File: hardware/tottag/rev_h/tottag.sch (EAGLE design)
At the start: 208 parts, among them J1 USB4110-GF-A, J2 DM3AT-SF-PEJM5, J3 TC2030-JLINK-NL-2SIDE, J4 TC2030-JLINK-NL-2SIDE, J5 MOLEX-PICO-SPOX-3SIDE, Q1 CSD75207W15, Q2 CSD75207W15, T1 HHM1595A1, U1 DW1000, U10 STM32F091CC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

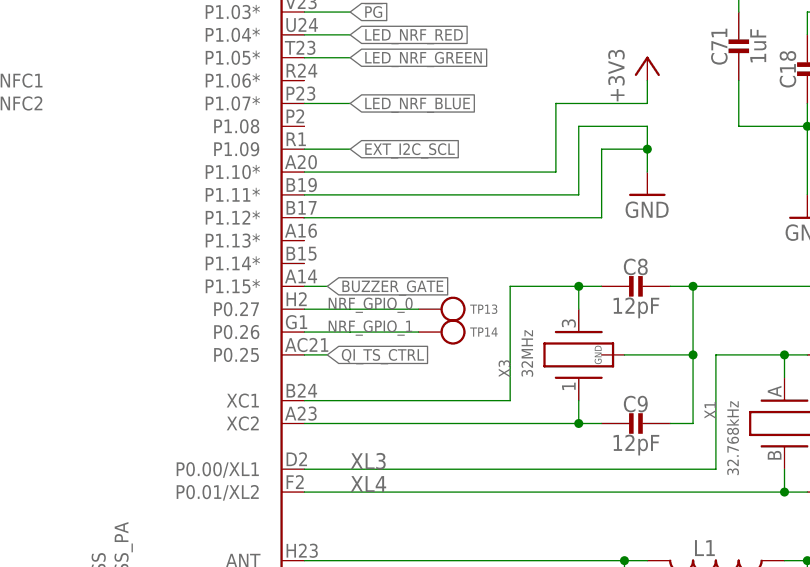
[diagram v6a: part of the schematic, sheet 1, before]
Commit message: rev_h: Connect STM PA0 to allow STANDBY wake
Slightly unclear whether STM should allow for STANDBY wake from any
of the WKUP pins, but some forum posts indicate that it can actually
only be done from WKUP1 for STANDBY mode. In either case, another
GPIO link between the two micro's isn't a huge deal.

This does sacrifice the GPIO1 test point from the nRF, because getting
at any other pin would've been insane.
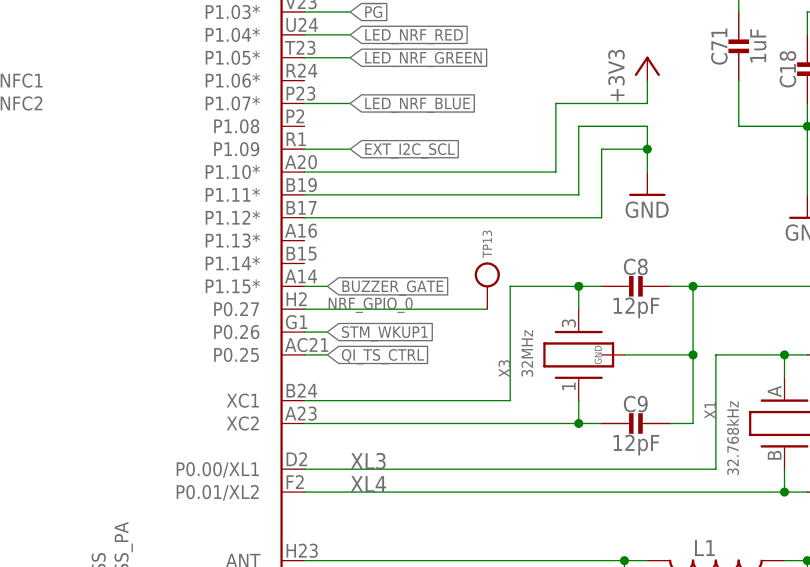
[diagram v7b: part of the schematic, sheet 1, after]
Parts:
- removed TP14: TEST-POINT, headers:TEST-POINT
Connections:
- removed net NRF_GPIO_1: TP14.TESTPOINT, U7.P0.26
- new net STM_WKUP1: U10.PA0, U7.P0.26
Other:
- note added: "Only PA0 can wake from STANDBY mode"
- moved on the sheet: TP13
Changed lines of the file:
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@@
 </part>
 <part name="TP13" library="headers" deviceset="TEST-POINT" device=""/>
-<part name="TP14" library="headers" deviceset="TEST-POINT" device=""/>
 <part name="FRAME3" library="lab11-frames" deviceset="LETTER_L_BLANK" device=""/>
 <part name="U10" library="chips" library_urn="urn:adsk.eagle:library:20878352" deviceset="STM32F091CC" device="" package3d_urn="urn:adsk.eagle:package:20878823/2"/>
@@
 <attribute name="VALUE" x="36.83" y="110.49" size="1.778" layer="96" ratio="12" rot="R270" align="bottom-center"/>
 </instance>
-<instance part="TP13" gate="G$1" x="121.92" y="68.58" smashed="yes" rot="R180">
-<attribute name="NAME" x="125.095" y="68.58" size="1.016" layer="95" ratio="12" rot="R180" align="center-right"/>
-</instance>
-<instance part="TP14" gate="G$1" x="121.92" y="66.04" smashed="yes" rot="R180">
-<attribute name="NAME" x="125.095" y="66.04" size="1.016" layer="95" ratio="12" rot="R180" align="center-right"/>
+<instance part="TP13" gate="G$1" x="127" y="71.12" smashed="yes" rot="R270">
+<attribute name="NAME" x="127" y="74.295" size="1.016" layer="95" ratio="12" rot="R270" align="center-right"/>
 </instance>
 <instance part="TP15" gate="G$1" x="96.52" y="144.78" smashed="yes" rot="R180">
@@
 </segment>
 </net>
-<net name="NRF_GPIO_1" class="0">
-<segment>
-<pinref part="U7" gate="G$1" pin="P0.26"/>
-<wire x1="106.68" y1="66.04" x2="111.76" y2="66.04" width="0.1524" layer="91"/>
-<pinref part="TP14" gate="G$1" pin="TESTPOINT"/>
-<wire x1="111.76" y1="66.04" x2="119.38" y2="66.04" width="0.1524" layer="91"/>
-<label x="109.22" y="66.04" size="1.27" layer="95"/>
-</segment>
-</net>
 <net name="NRF_GPIO_0" class="0">
 <segment>
 <pinref part="U7" gate="G$1" pin="P0.27"/>
-<wire x1="106.68" y1="68.58" x2="111.76" y2="68.58" width="0.1524" layer="91"/>
 <pinref part="TP13" gate="G$1" pin="TESTPOINT"/>
-<wire x1="111.76" y1="68.58" x2="119.38" y2="68.58" width="0.1524" layer="91"/>
+<wire x1="106.68" y1="68.58" x2="127" y2="68.58" width="0.1524" layer="91"/>
 <label x="109.22" y="68.58" size="1.27" layer="95"/>
 </segment>
@@
 </segment>
 </net>
+<net name="STM_WKUP1" class="0">
+<segment>
+<pinref part="U7" gate="G$1" pin="P0.26"/>
+<wire x1="109.22" y1="66.04" x2="106.68" y2="66.04" width="0.1524" layer="91"/>
+<label x="109.22" y="66.04" size="1.27" layer="95" xref="yes"/>
+</segment>
+</net>
 </nets>
 </sheet>
@@
 <text x="38.1" y="2.54" size="2.032" layer="98" rot="R180" align="center">2x Programming header (top/bot)</text>
 <text x="151.13" y="87.63" size="1.27" layer="98" rot="R90">1% tol</text>
+<text x="71.12" y="132.334" size="0.762" layer="98">Only PA0 can wake from STANDBY mode</text>
 </plain>
 <instances>
@@
 </segment>
 </net>
+<net name="STM_WKUP1" class="0">
+<segment>
+<pinref part="U10" gate="U1" pin="PA0"/>
+<wire x1="71.12" y1="106.68" x2="71.12" y2="132.08" width="0.1524" layer="91"/>
+<wire x1="71.12" y1="132.08" x2="111.76" y2="132.08" width="0.1524" layer="91"/>
+<label x="111.76" y="132.08" size="1.27" layer="95" xref="yes"/>
+</segment>
+</net>

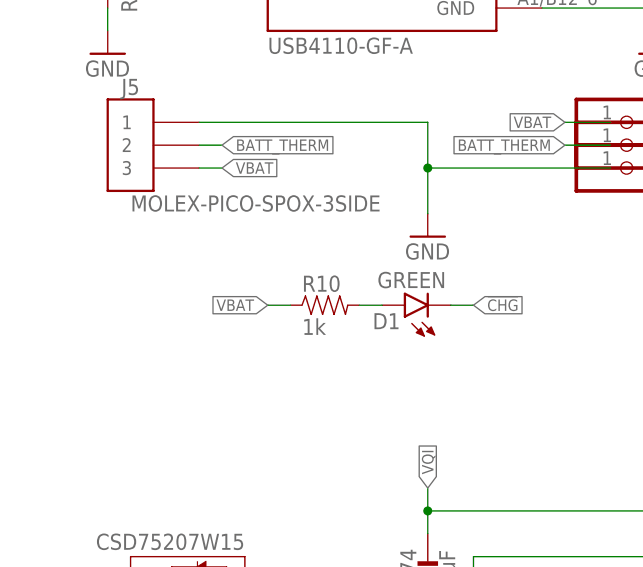
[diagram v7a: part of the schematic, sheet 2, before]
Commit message: rev_h: tie !CHG LED to +3v3
This means the LED won't power on to indicate charging if the device
is switched off, but that's an uncommon case anyway. We may even end
up just DNP'ing the CHG LED; it's of middling use; in which case an
internal nRF pull-up can be used in place of this for the !CHG net.
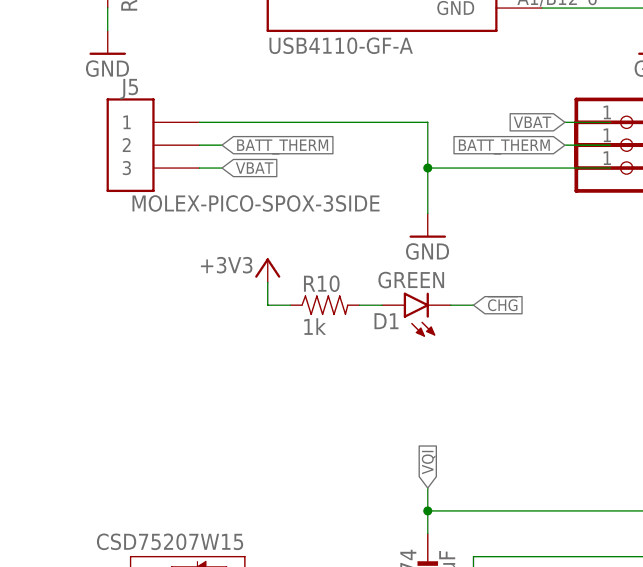
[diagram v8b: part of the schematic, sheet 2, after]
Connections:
- net +3V3: now also R10.1
- net VBAT: no longer R10.1
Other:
- note added: "Caution: The !CHG network connects to a GPIO pin on the nRF, which can leak power through the ESD pins when the nRF is not energized (i.e. don't drive this LED from VBAT!)"
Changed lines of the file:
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@@
 <part name="TP26" library="headers" deviceset="TEST-POINT" device=""/>
 <part name="TP27" library="headers" deviceset="TEST-POINT" device=""/>
+<part name="P+8" library="regulators" deviceset="+3V3" device=""/>
 </parts>
 <sheets>
@@
 the connector (metal contacts of the connector
 not visible), the wires from L to R are [-, NTC, +]</text>
+<text x="24.384" y="124.206" size="0.8128" layer="98" align="top-right">Caution: The !CHG network
+connects to a GPIO pin on the
+nRF, which can leak power
+through the ESD pins when the
+nRF is not energized (i.e. don't
+drive this LED from VBAT!)</text>
 </plain>
 <instances>
@@
 <attribute name="NAME" x="68.326" y="137.287" size="1.778" layer="95"/>
 <attribute name="VALUE" x="59.69" y="132.08" size="1.778" layer="96"/>
+</instance>
+<instance part="P+8" gate="P1" x="25.4" y="127" smashed="yes">
+<attribute name="VALUE" x="23.876" y="127.254" size="1.778" layer="96" rot="R180"/>
 </instance>
 </instances>
@@
 <wire x1="20.32" y1="33.02" x2="15.24" y2="33.02" width="0.1524" layer="91"/>
 </segment>
+<segment>
+<pinref part="R10" gate="G$1" pin="1"/>
+<wire x1="27.94" y1="121.92" x2="25.4" y2="121.92" width="0.1524" layer="91"/>
+<wire x1="25.4" y1="121.92" x2="25.4" y2="124.46" width="0.1524" layer="91"/>
+<pinref part="P+8" gate="P1" pin="+3V3"/>
+</segment>
 </net>
 <net name="VBAT" class="0">
@@
 </segment>
 <segment>
-<pinref part="R10" gate="G$1" pin="1"/>
-<wire x1="25.4" y1="121.92" x2="27.94" y2="121.92" width="0.1524" layer="91"/>
-<label x="25.4" y="121.92" size="1.27" layer="95" rot="R180" xref="yes"/>
-</segment>
-<segment>
